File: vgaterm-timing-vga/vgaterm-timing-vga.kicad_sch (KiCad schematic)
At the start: 48 parts, among them J1 Conn_01x15, J2 Conn_01x08, J3 DE15_Receptacle_HighDensity_M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, J4 Conn_01x03_Pin, J5 Conn_01x02_Pin, J6 Conn_01x03_Pin, J7 Conn_01x02_Pin, U1 74LS161, U2 74LS161, U3 28C256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

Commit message: updating board based on convos with Seth
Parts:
- added J8: Conn_01x04, Connector_Molex:Molex_PicoBlade_53261-0471_1x04-1MP_P1.25mm_Horizontal, symbol Connector_Generic:Conn_01x04
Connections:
- net B2: now also J8.1 (Pin_1)
- net G2: now also J8.2 (Pin_2)
- net GND: now also J8.4 (Pin_4); no longer U9.6 (D4), U9.7 (D5)
- net HSYNC_{2}: now also U9.6 (D4); no longer J3.13, U9.17 (Q2)
- net R2: now also J8.3 (Pin_3)
- net VSYNC_{2}: now also U9.7 (D5); no longer J3.14, U9.16 (Q3)
- new net HSYNC_{3}: J3.13, U9.17 (Q2)
- new net VSYNC_{3}: J3.14, U9.16 (Q3)
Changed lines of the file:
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@@
   (junction (at 257.81 49.53) (diameter 0) (color 0 0 0 0)
   )
-  (junction (at 245.11 72.39) (diameter 0) (color 0 0 0 0)
-  )
   (junction (at 185.42 99.06) (diameter 0) (color 0 0 0 0)
   )
@@
   (junction (at 260.35 139.7) (diameter 0) (color 0 0 0 0)
   )
-  (junction (at 245.11 69.85) (diameter 0) (color 0 0 0 0)
-  )
   (junction (at 160.02 143.51) (diameter 0) (color 0 0 0 0)
   )
@@
     (stroke (width 0) (type default))
   )
-  (wire (pts (xy 245.11 67.31) (xy 245.11 69.85))
-    (stroke (width 0) (type default))
-  )
   (wire (pts (xy 185.42 97.79) (xy 185.42 99.06))
     (stroke (width 0) (type default))
@@
     (stroke (width 0) (type default))
   )
-  (wire (pts (xy 245.11 69.85) (xy 245.11 72.39))
-    (stroke (width 0) (type default))
-  )
   (wire (pts (xy 130.81 68.58) (xy 133.35 68.58))
     (stroke (width 0) (type default))
@@
     (effects (font (size 1.27 1.27)) (justify left bottom))
   )
-  (label "VSYNC_{2}" (at 81.28 91.44 90) (fields_autoplaced)
-    (effects (font (size 1.27 1.27)) (justify left bottom))
-  )
   (label "CLK_{sync}" (at 250.19 106.68 0) (fields_autoplaced)
     (effects (font (size 1.27 1.27)) (justify left bottom))
@@
     (effects (font (size 1.27 1.27)) (justify left bottom))
   )
+  (label "VSYNC_{3}" (at 81.28 91.44 90) (fields_autoplaced)
+    (effects (font (size 1.27 1.27)) (justify left bottom))
+  )
   (label "Vis" (at 26.67 29.21 0) (fields_autoplaced)
     (effects (font (size 1.27 1.27)) (justify left bottom))
@@
     (effects (font (size 1.27 1.27)) (justify left bottom))
   )
+  (label "R2" (at 99.06 54.61 180) (fields_autoplaced)
+    (effects (font (size 1.27 1.27)) (justify right bottom))
+  )
   (label "P3" (at 26.67 49.53 0) (fields_autoplaced)
     (effects (font (size 1.27 1.27)) (justify left bottom))
@@
     (effects (font (size 1.27 1.27)) (justify right bottom))
   )
+  (label "HSYNC_{3}" (at 76.2 91.44 90) (fields_autoplaced)
+    (effects (font (size 1.27 1.27)) (justify left bottom))
+  )
+  (label "G2" (at 99.06 52.07 180) (fields_autoplaced)
+    (effects (font (size 1.27 1.27)) (justify right bottom))
+  )
   (label "A14" (at 130.81 91.44 0) (fields_autoplaced)
     (effects (font (size 1.27 1.27)) (justify left bottom))
@@
     (effects (font (size 1.27 1.27)) (justify left bottom))
   )
+  (label "HSYNC_{3}" (at 270.51 62.23 0) (fields_autoplaced)
+    (effects (font (size 1.27 1.27)) (justify left bottom))
+  )
   (label "P6" (at 77.47 27.94 90) (fields_autoplaced)
     (effects (font (size 1.27 1.27)) (justify left bottom))
@@
     (effects (font (size 1.27 1.27)) (justify left bottom))
   )
-  (label "HSYNC_{2}" (at 270.51 62.23 0) (fields_autoplaced)
-    (effects (font (size 1.27 1.27)) (justify left bottom))
+  (label "HSYNC_{2}" (at 245.11 67.31 180) (fields_autoplaced)
+    (effects (font (size 1.27 1.27)) (justify right bottom))
   )
   (label "A12" (at 130.81 86.36 0) (fields_autoplaced)
@@
     (effects (font (size 1.27 1.27)) (justify left bottom))
   )
-  (label "VSYNC_{2}" (at 270.51 64.77 0) (fields_autoplaced)
-    (effects (font (size 1.27 1.27)) (justify left bottom))
+  (label "VSYNC_{2}" (at 245.11 69.85 180) (fields_autoplaced)
+    (effects (font (size 1.27 1.27)) (justify right bottom))
   )
   (label "A1" (at 130.81 58.42 0) (fields_autoplaced)
@@
     (effects (font (size 1.27 1.27)) (justify left bottom))
   )
-  (label "HSYNC_{2}" (at 76.2 91.44 90) (fields_autoplaced)
-    (effects (font (size 1.27 1.27)) (justify left bottom))
-  )
   (label "A6" (at 130.81 71.12 0) (fields_autoplaced)
     (effects (font (size 1.27 1.27)) (justify left bottom))
@@
     (effects (font (size 1.27 1.27)) (justify left bottom))
   )
+  (label "B2" (at 99.06 49.53 180) (fields_autoplaced)
+    (effects (font (size 1.27 1.27)) (justify right bottom))
+  )
+  (label "VSYNC_{3}" (at 270.51 64.77 0) (fields_autoplaced)
+    (effects (font (size 1.27 1.27)) (justify left bottom))
+  )
   (symbol (lib_id "Device:R") (at 80.01 72.39 90) (unit 1)
     (in_bom yes) (on_board yes) (dnp no) (fields_autoplaced)
@@
     )
   )
+  (symbol (lib_id "power:GND") (at 99.06 57.15 0) (unit 1)
+    (in_bom yes) (on_board yes) (dnp no) (fields_autoplaced)
+    (property "Reference" "#PWR055" (at 99.06 63.5 0)
+      (effects (font (size 1.27 1.27)) hide)
+    )
+    (property "Value" "GND" (at 99.06 62.23 0)
+      (effects (font (size 1.27 1.27)))
+    )
+    (property "Footprint" "" (at 99.06 57.15 0)
+      (effects (font (size 1.27 1.27)) hide)
+    )
+    (property "Datasheet" "" (at 99.06 57.15 0)
+      (effects (font (size 1.27 1.27)) hide)
+    )
+    (pin "1")
+    (instances
+      (project "vgaterm-timing-vga"
+        (path "/2507db06-1687-4aca-8562-74daa0e6a71c"
+          (reference "#PWR055") (unit 1)
+        )
+      )
+      (project "vga-connection"
+        (path "/96e66b69-8426-4b51-b32a-8435b751d1a6"
+          (reference "#PWR04") (unit 1)
+        )
+      )
+    )
+  )
   (symbol (lib_id "Device:R") (at 72.39 72.39 90) (unit 1)
     (in_bom yes) (on_board yes) (dnp no) (fields_autoplaced)
@@
         )
       )
+    )
+  )
+  (symbol (lib_id "Connector_Generic:Conn_01x04") (at 104.14 52.07 0) (unit 1)
+    (in_bom yes) (on_board yes) (dnp no) (fields_autoplaced)
+    (property "Reference" "J8" (at 106.68 52.07 0)
+      (effects (font (size 1.27 1.27)) (justify left))
+    )
+    (property "Value" "Conn_01x04" (at 106.68 54.61 0)
+      (effects (font (size 1.27 1.27)) (justify left))
+    )
+    (property "Footprint" "Connector_Molex:Molex_PicoBlade_53261-0471_1x04-1MP_P1.25mm_Horizontal" (at 104.14 52.07 0)
+      (effects (font (size 1.27 1.27)) hide)
+    )
+    (property "Datasheet" "~" (at 104.14 52.07 0)
+      (effects (font (size 1.27 1.27)) hide)
+    )
+    (pin "1")
+    (pin "2")
+    (pin "3")
+    (pin "4")
+    (instances
+      (project "vgaterm-timing-vga"
+        (path "/2507db06-1687-4aca-8562-74daa0e6a71c"
+          (reference "J8") (unit 1)
+        )
+      )

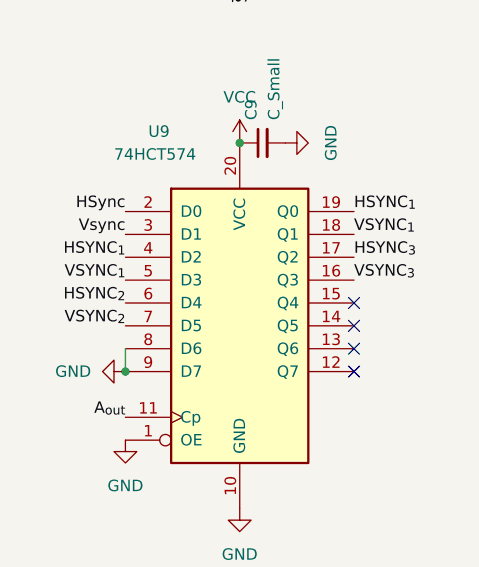
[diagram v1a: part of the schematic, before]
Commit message: updating timing board hsync vsync delay
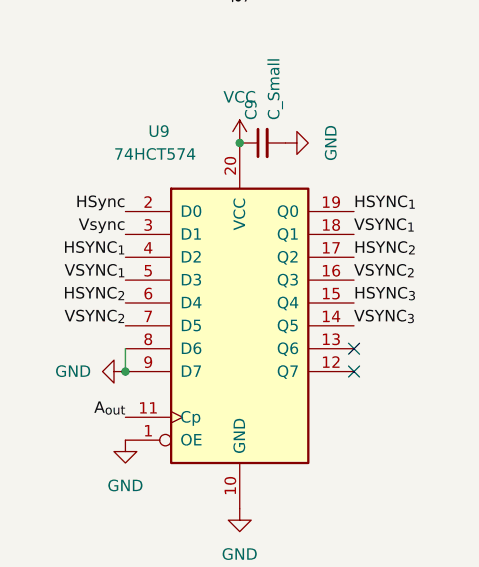
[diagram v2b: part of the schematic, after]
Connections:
- net HSYNC_{2}: now also U9.17 (Q2)
- net HSYNC_{3}: now also U9.15 (Q4); no longer U9.17 (Q2)
- net VSYNC_{2}: now also U9.16 (Q3)
- net VSYNC_{3}: now also U9.14 (Q5); no longer U9.16 (Q3)
- no-connect marks 24 -> 22
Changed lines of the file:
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@@
   (no_connect (at 247.65 110.49))
   (no_connect (at 59.69 27.94))
-  (no_connect (at 270.51 69.85))
   (no_connect (at 57.15 53.34))
   (no_connect (at 270.51 72.39))
@@
   (no_connect (at 71.12 91.44))
   (no_connect (at 82.55 53.34))
-  (no_connect (at 270.51 67.31))
   (wire (pts (xy 20.32 135.89) (xy 20.32 143.51))
     (stroke (width 0) (type default))
@@
     (effects (font (size 1.27 1.27)) (justify left bottom))
   )
-  (label "HSYNC_{3}" (at 270.51 62.23 0) (fields_autoplaced)
+  (label "HSYNC_{3}" (at 270.51 67.31 0) (fields_autoplaced)
     (effects (font (size 1.27 1.27)) (justify left bottom))
   )
@@
     (effects (font (size 1.27 1.27)) (justify left bottom))
   )
+  (label "HSYNC_{2}" (at 245.11 67.31 180) (fields_autoplaced)
+    (effects (font (size 1.27 1.27)) (justify right bottom))
+  )
   (label "~{RESET}" (at 160.02 99.06 0) (fields_autoplaced)
     (effects (font (size 1.27 1.27)) (justify left bottom))
@@
     (effects (font (size 1.27 1.27)) (justify left bottom))
   )
-  (label "HSYNC_{2}" (at 245.11 67.31 180) (fields_autoplaced)
-    (effects (font (size 1.27 1.27)) (justify right bottom))
+  (label "HSYNC_{2}" (at 270.51 62.23 0) (fields_autoplaced)
+    (effects (font (size 1.27 1.27)) (justify left bottom))
   )
   (label "A12" (at 130.81 86.36 0) (fields_autoplaced)
@@
     (effects (font (size 1.27 1.27)) (justify right bottom))
   )
+  (label "VSYNC_{2}" (at 245.11 69.85 180) (fields_autoplaced)
+    (effects (font (size 1.27 1.27)) (justify right bottom))
+  )
   (label "HSync" (at 245.11 57.15 180) (fields_autoplaced)
     (effects (font (size 1.27 1.27)) (justify right bottom))
@@
     (effects (font (size 1.27 1.27)) (justify left bottom))
   )
-  (label "VSYNC_{2}" (at 245.11 69.85 180) (fields_autoplaced)
-    (effects (font (size 1.27 1.27)) (justify right bottom))
+  (label "VSYNC_{2}" (at 270.51 64.77 0) (fields_autoplaced)
+    (effects (font (size 1.27 1.27)) (justify left bottom))
   )
   (label "A1" (at 130.81 58.42 0) (fields_autoplaced)
@@
     (effects (font (size 1.27 1.27)) (justify right bottom))
   )
-  (label "VSYNC_{3}" (at 270.51 64.77 0) (fields_autoplaced)
-    (effects (font (size 1.27 1.27)) (justify left bottom))
-  )
+  (label "VSYNC_{3}" (at 270.51 69.85 0) (fields_autoplaced)
+    (effects (font (size 1.27 1.27)) (justify left bottom))
+  )

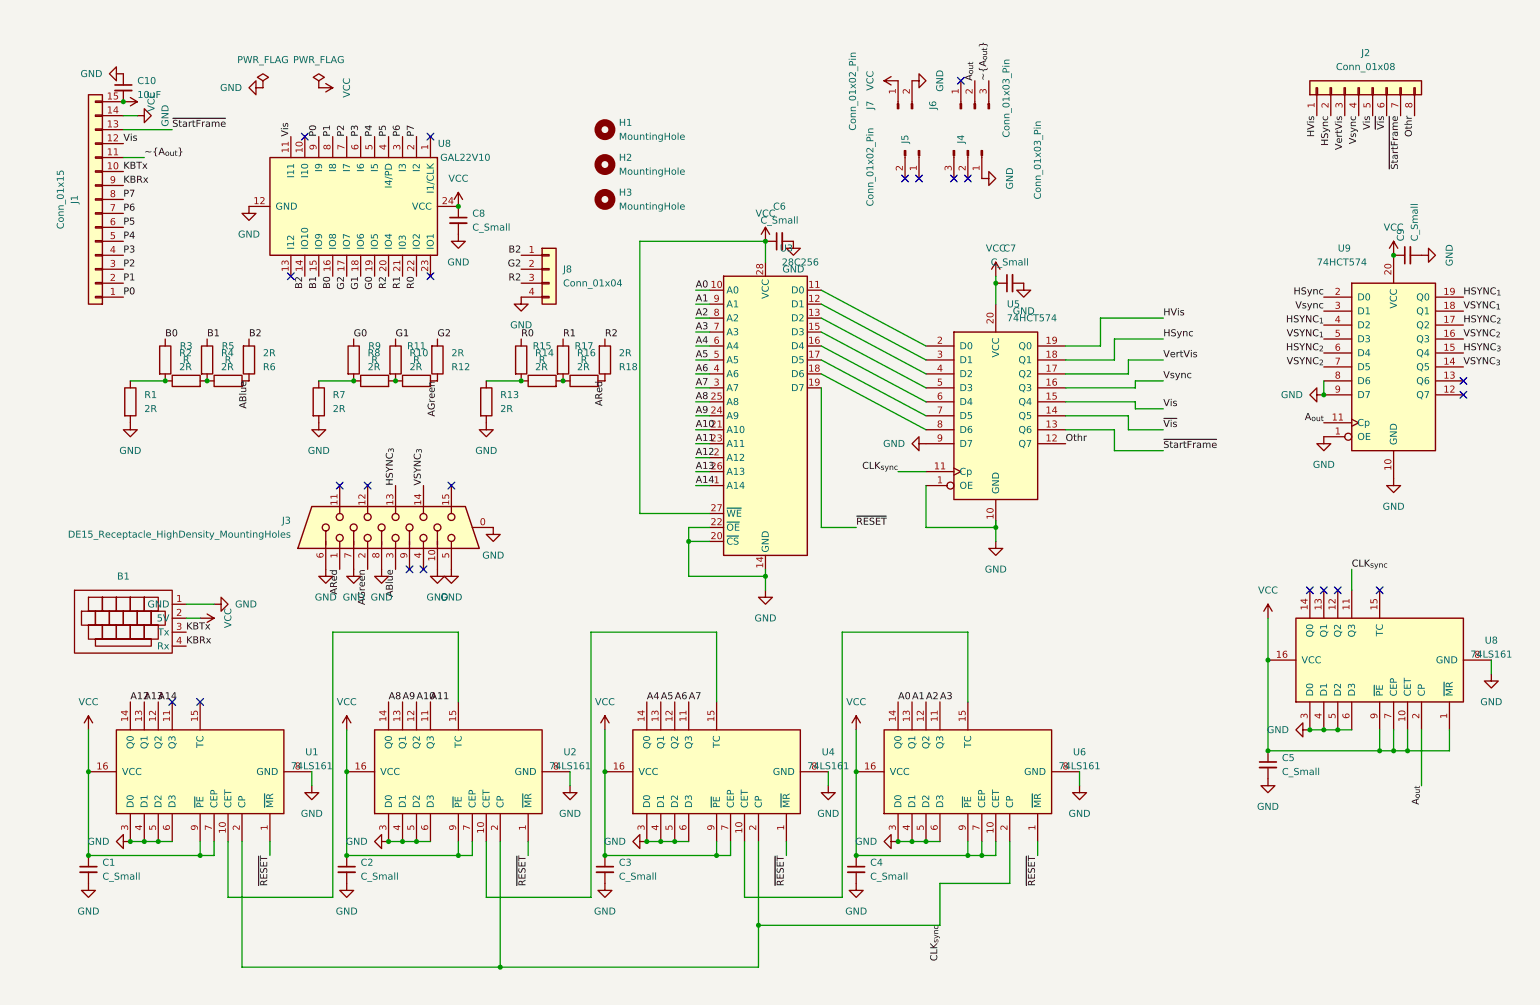
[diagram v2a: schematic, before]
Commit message: timing board updates and adding keyboard loft board and vga breakout
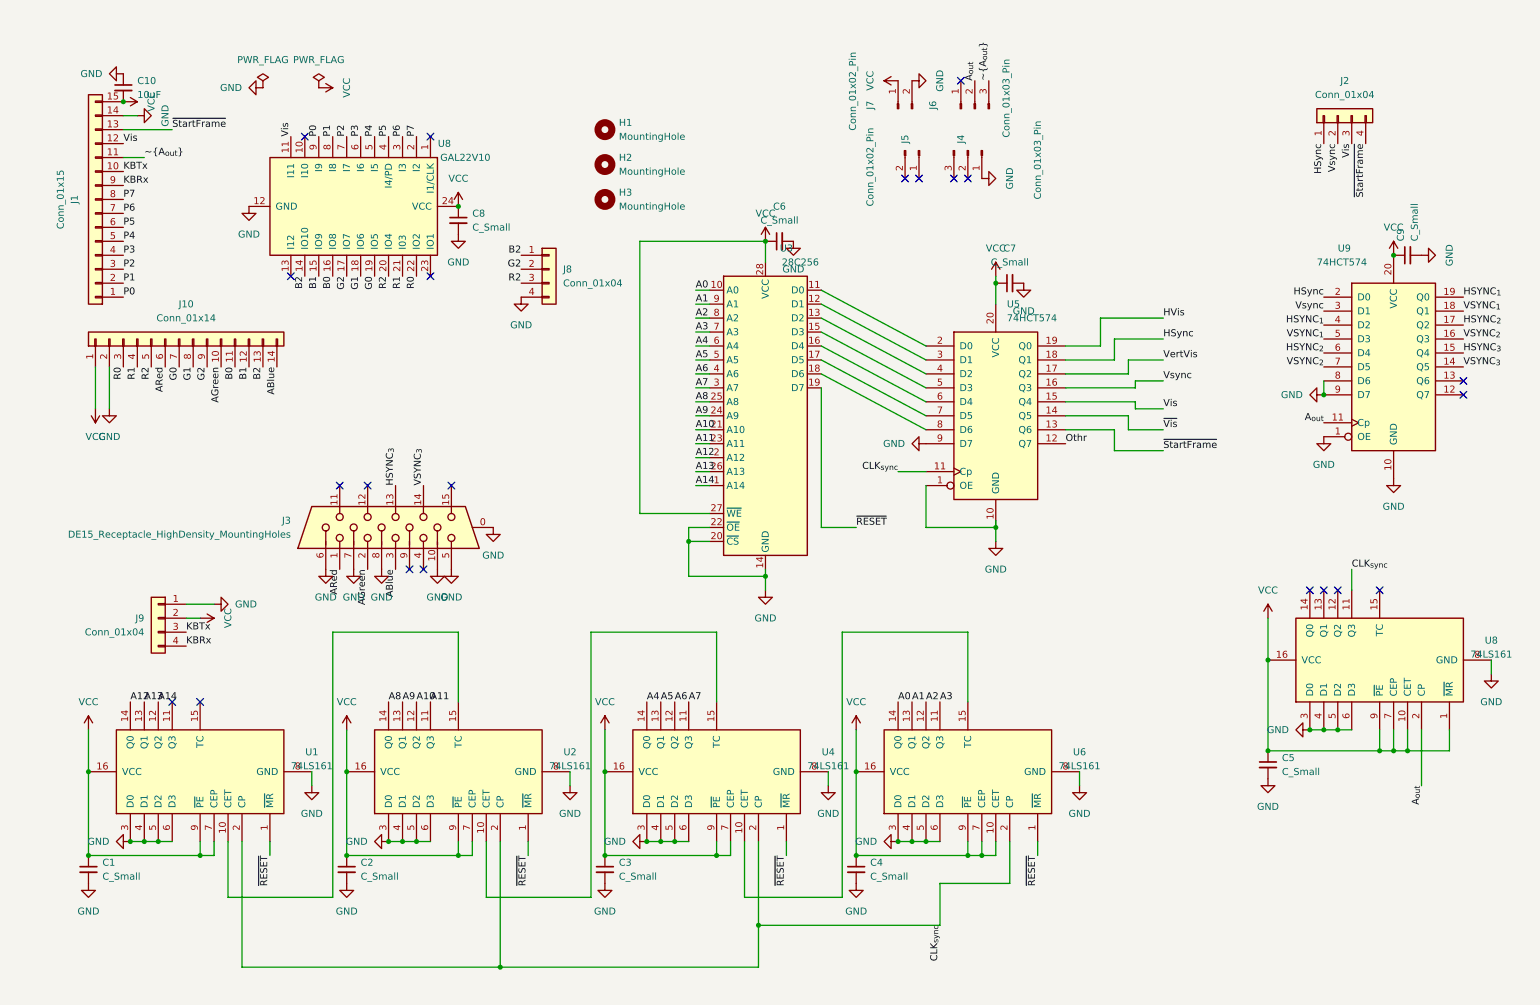
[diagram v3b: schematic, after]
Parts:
- removed B1: ~, local:USB-UART-board, symbol local:KB-UART-board
- removed J2: Conn_01x08, local:M208890845, symbol Connector_Generic:Conn_01x08
- removed R1, R10, R12, R13, R14, R16, R18, R2, R4, R6, R7, R8: 2R, Resistor_SMD:R_0805_2012Metric_Pad1.20x1.40mm_HandSolder, symbol Device:R
- removed R11, R15, R17, R3, R5, R9: R, Resistor_SMD:R_0805_2012Metric_Pad1.20x1.40mm_HandSolder, symbol Device:R
- added J10: Conn_01x14, Connector_PinSocket_2.54mm:PinSocket_1x14_P2.54mm_Vertical_SMD_Pin1Left, symbol Connector_Generic:Conn_01x14
- added J2: Conn_01x04, Connector_PinHeader_2.54mm:PinHeader_2x02_P2.54mm_Vertical_SMD, symbol Connector_Generic:Conn_01x04
- added J9: Conn_01x04, Connector_PinSocket_2.54mm:PinSocket_2x02_P2.54mm_Vertical, symbol Connector_Generic:Conn_01x04
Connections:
- net ABlue: now also J10.14 (Pin_14)
- net AGreen: now also J10.10 (Pin_10)
- net ARed: now also J10.6 (Pin_6)
- net B0: now also J10.11 (Pin_11)
- net B1: now also J10.12 (Pin_12)
- net B2: now also J10.13 (Pin_13)
- net G0: now also J10.7 (Pin_7)
- net G1: now also J10.8 (Pin_8)
- net G2: now also J10.9 (Pin_9)
- net GND: now also J10.2 (Pin_2), J9.1 (Pin_1)
- net HSync: now also J2.1 (Pin_1)
- net KBRx: now also J9.4 (Pin_4)
- net KBTx: now also J9.3 (Pin_3)
- net R0: now also J10.3 (Pin_3)
- net R1: now also J10.4 (Pin_4)
- net R2: now also J10.5 (Pin_5)
- net VCC: now also J10.1 (Pin_1), J9.2 (Pin_2)
- net Vis: now also J2.3 (Pin_3)
- net Vsync: now also J2.2 (Pin_2)
- net ~{StartFrame}: now also J2.4 (Pin_4)

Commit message: current boards
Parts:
- J3: footprint Connector_Dsub:DSUB-15-HD_Female_Horizontal_P2.29x1.98mm_EdgePinOffset8.35mm_Housed_MountingHolesOffset10.89mm -> local:DSUB-15-HD_Female_Horizontal_P2.29x2.54mm_EdgePinOffset8.35mm_Housed_MountingHolesOffset10.89mm
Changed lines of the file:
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@@
       (effects (font (size 1.27 1.27)) (justify left))
     )
-    (property "Footprint" "Connector_Dsub:DSUB-15-HD_Female_Horizontal_P2.29x1.98mm_EdgePinOffset8.35mm_Housed_MountingHolesOffset10.89mm" (at 66.04 123.19 0)
+    (property "Footprint" "local:DSUB-15-HD_Female_Horizontal_P2.29x2.54mm_EdgePinOffset8.35mm_Housed_MountingHolesOffset10.89mm" (at 66.04 123.19 0)
       (effects (font (size 1.27 1.27)) hide)
     )
